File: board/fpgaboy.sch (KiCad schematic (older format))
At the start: 83 parts, among them J1 Conn_01x12, J2 Conn_01x06, J3 Micro_SD_Card_Det, J4 Conn_01x06, P1 ILI9341, P2 CONN_01X02, P3 USB_OTG, Q1 BSS816NW, SW1 SWITCH_SPST, U1 iCE40-HX8k-BG121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

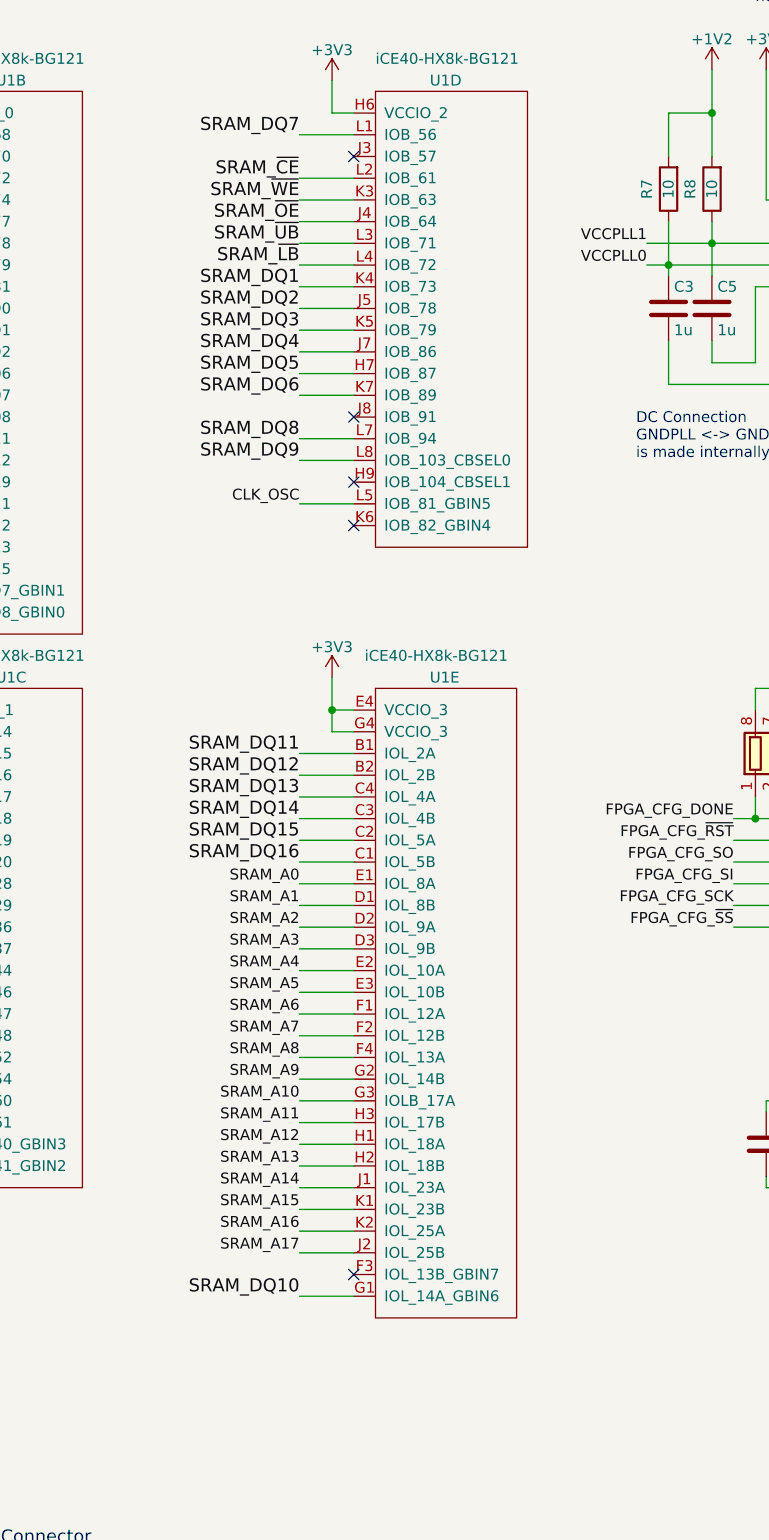
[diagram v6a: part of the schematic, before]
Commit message: Pin-swapping + routing the SRAM: 50%
Former-commit-id: 2b577cf7b52f24baabab8caba00ed91606b61012 [formerly dccfe95725d7621aa8f631ef6b86a4224c43d36a]
Former-commit-id: 66db710dd59c402621ba8271397dc92d027909e4
Former-commit-id: c62c4198c05e169013effc5fdc660d776587b68b
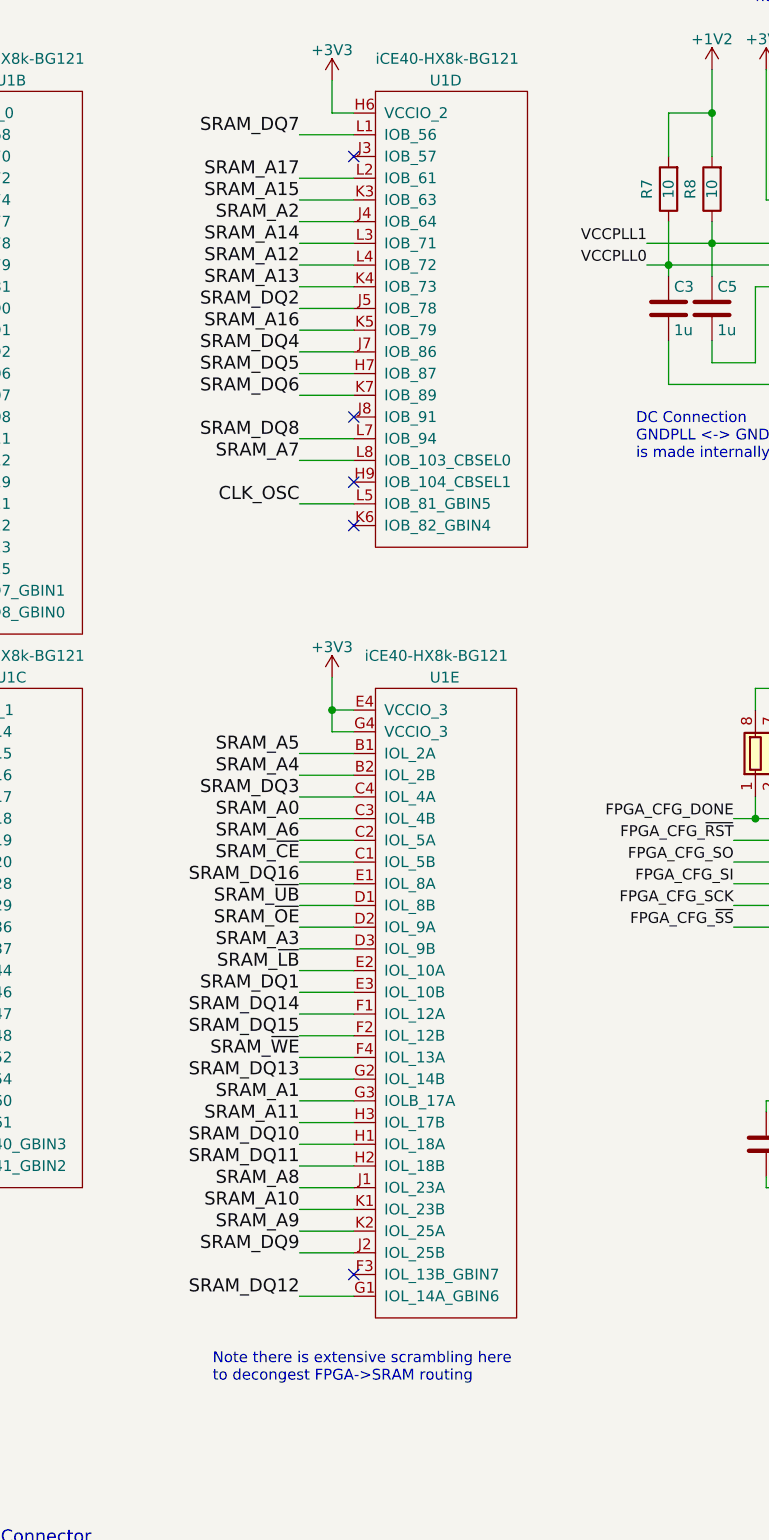
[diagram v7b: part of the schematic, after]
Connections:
- net SRAM_A0: now also U1.C3 (IOL_4B); no longer U1.E1 (IOL_8A)
- net SRAM_A1: now also U1.G3 (IOLB_17A); no longer U1.D1 (IOL_8B)
- net SRAM_A10: now also U1.K1 (IOL_23B); no longer U1.G3 (IOLB_17A)
- net SRAM_A12: now also U1.L4 (IOB_72); no longer U1.H1 (IOL_18A)
- net SRAM_A13: now also U1.K4 (IOB_73); no longer U1.H2 (IOL_18B)
- net SRAM_A14: now also U1.L3 (IOB_71); no longer U1.J1 (IOL_23A)
- net SRAM_A15: now also U1.K3 (IOB_63); no longer U1.K1 (IOL_23B)
- net SRAM_A16: now also U1.K5 (IOB_79); no longer U1.K2 (IOL_25A)
- net SRAM_A17: now also U1.L2 (IOB_61); no longer U1.J2 (IOL_25B)
- net SRAM_A2: now also U1.J4 (IOB_64); no longer U1.D2 (IOL_9A)
- net SRAM_A4: now also U1.B2 (IOL_2B); no longer U1.E2 (IOL_10A)
- net SRAM_A5: now also U1.B1 (IOL_2A); no longer U1.E3 (IOL_10B)
- net SRAM_A6: now also U1.C2 (IOL_5A); no longer U1.F1 (IOL_12A)
- net SRAM_A7: now also U1.L8 (IOB_103_CBSEL0); no longer U1.F2 (IOL_12B)
- net SRAM_A8: now also U1.J1 (IOL_23A); no longer U1.F4 (IOL_13A)
- net SRAM_A9: now also U1.K2 (IOL_25A); no longer U1.G2 (IOL_14B)
- net SRAM_DQ1: now also U1.E3 (IOL_10B); no longer U1.K4 (IOB_73)
- net SRAM_DQ10: now also U1.H1 (IOL_18A); no longer U1.G1 (IOL_14A_GBIN6)
- net SRAM_DQ11: now also U1.H2 (IOL_18B); no longer U1.B1 (IOL_2A)
- net SRAM_DQ12: now also U1.G1 (IOL_14A_GBIN6); no longer U1.B2 (IOL_2B)
- net SRAM_DQ13: now also U1.G2 (IOL_14B); no longer U1.C4 (IOL_4A)
- net SRAM_DQ14: now also U1.F1 (IOL_12A); no longer U1.C3 (IOL_4B)
- net SRAM_DQ15: now also U1.F2 (IOL_12B); no longer U1.C2 (IOL_5A)
- net SRAM_DQ16: now also U1.E1 (IOL_8A); no longer U1.C1 (IOL_5B)
- net SRAM_DQ3: now also U1.C4 (IOL_4A); no longer U1.K5 (IOB_79)
- net SRAM_DQ9: now also U1.J2 (IOL_25B); no longer U1.L8 (IOB_103_CBSEL0)
- net SRAM_~CE: now also U1.C1 (IOL_5B); no longer U1.L2 (IOB_61)
- net SRAM_~LB: now also U1.E2 (IOL_10A); no longer U1.L4 (IOB_72)
- net SRAM_~OE: now also U1.D2 (IOL_9A); no longer U1.J4 (IOB_64)
- net SRAM_~UB: now also U1.D1 (IOL_8B); no longer U1.L3 (IOB_71)
- net SRAM_~WE: now also U1.F4 (IOL_13A); no longer U1.K3 (IOB_63)
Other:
- note added: "Note there is extensive scrambling here\nto decongest FPGA->SRAM routing"
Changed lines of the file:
@@
 	1    0    0    -1
 $EndComp
-Text Label 3300 4350 2    60   ~ 0
+Text Label 3300 6250 2    60   ~ 0
 SRAM_DQ11
-Text Label 3300 4450 2    60   ~ 0
+Text Label 3300 6850 2    60   ~ 0
 SRAM_DQ12
-Text Label 3300 4550 2    60   ~ 0
+Text Label 3300 5850 2    60   ~ 0
 SRAM_DQ13
-Text Label 3300 4650 2    60   ~ 0
+Text Label 3300 5550 2    60   ~ 0
 SRAM_DQ14
-Text Label 3300 4750 2    60   ~ 0
+Text Label 3300 5650 2    60   ~ 0
 SRAM_DQ15
-Text Label 3300 4850 2    60   ~ 0
+Text Label 3300 4950 2    60   ~ 0
 SRAM_DQ16
 Wire Wire Line
@@
 	1    0    0    -1
 $EndComp
-Text Label 3300 2200 2    60   ~ 0
+Text Label 3300 5450 2    60   ~ 0
 SRAM_DQ1
 Text Label 3300 2300 2    60   ~ 0
 SRAM_DQ2
-Text Label 3300 2400 2    60   ~ 0
+Text Label 3300 4550 2    60   ~ 0
 SRAM_DQ3
 Text Label 3300 2500 2    60   ~ 0
@@
 Text Label 3300 2900 2    60   ~ 0
 SRAM_DQ8
-Text Label 3300 3000 2    60   ~ 0
+Text Label 3300 6650 2    60   ~ 0
 SRAM_DQ9
-Text Label 3300 6850 2    60   ~ 0
+Text Label 3300 6150 2    60   ~ 0
 SRAM_DQ10
 Wire Wire Line
@@
 Wire Wire Line
 	3550 6650 3300 6650
-Text Label 3300 4950 2    50   ~ 0
+Text Label 3300 4650 2    60   ~ 0
 SRAM_A0
-Text Label 3300 5050 2    50   ~ 0
+Text Label 3300 5950 2    60   ~ 0
 SRAM_A1
-Text Label 3300 5150 2    50   ~ 0
+Text Label 3300 1900 2    60   ~ 0
 SRAM_A2
-Text Label 3300 5250 2    50   ~ 0
+Text Label 3300 5250 2    60   ~ 0
 SRAM_A3
-Text Label 3300 5350 2    50   ~ 0
+Text Label 3300 4450 2    60   ~ 0
 SRAM_A4
-Text Label 3300 5450 2    50   ~ 0
+Text Label 3300 4350 2    60   ~ 0
 SRAM_A5
-Text Label 3300 5550 2    50   ~ 0
+Text Label 3300 4750 2    60   ~ 0
 SRAM_A6
-Text Label 3300 5650 2    50   ~ 0
+Text Label 3300 3000 2    60   ~ 0
 SRAM_A7
-Text Label 3300 5750 2    50   ~ 0
+Text Label 3300 6350 2    60   ~ 0
 SRAM_A8
-Text Label 3300 5850 2    50   ~ 0
+Text Label 3300 6550 2    60   ~ 0
 SRAM_A9
-Text Label 3300 5950 2    50   ~ 0
+Text Label 3300 6450 2    60   ~ 0
 SRAM_A10
-Text Label 3300 6050 2    50   ~ 0
+Text Label 3300 6050 2    60   ~ 0
 SRAM_A11
-Text Label 3300 6150 2    50   ~ 0
+Text Label 3300 2100 2    60   ~ 0
 SRAM_A12
-Text Label 3300 6250 2    50   ~ 0
+Text Label 3300 2200 2    60   ~ 0
 SRAM_A13
-Text Label 3300 6350 2    50   ~ 0
+Text Label 3300 2000 2    60   ~ 0
 SRAM_A14
-Text Label 3300 6450 2    50   ~ 0
+Text Label 3300 1800 2    60   ~ 0
 SRAM_A15
-Text Label 3300 6550 2    50   ~ 0
+Text Label 3300 2400 2    60   ~ 0
 SRAM_A16
-Text Label 3300 6650 2    50   ~ 0
+Text Label 3300 1700 2    60   ~ 0
 SRAM_A17
 Text Label 1350 4350 2    59   ~ 0
@@
 Wire Wire Line
 	3550 3200 3300 3200
-Text Label 3300 3200 2    50   ~ 0
+Text Label 3300 3200 2    60   ~ 0
 CLK_OSC
 NoConn ~ 3550 1600
@@
 Text Notes 6650 3550 0    50   ~ 0
 Separate nets from 1V2\ndue to RC filter. Must\nexplicitly mark as powered.
-Text Label 3300 1700 2    60   ~ 0
+Text Label 3300 4850 2    60   ~ 0
 SRAM_~CE
-Text Label 3300 1800 2    60   ~ 0
+Text Label 3300 5750 2    60   ~ 0
 SRAM_~WE
-Text Label 3300 1900 2    60   ~ 0
+Text Label 3300 5150 2    60   ~ 0
 SRAM_~OE
-Text Label 3300 2000 2    60   ~ 0
+Text Label 3300 5050 2    60   ~ 0
 SRAM_~UB
-Text Label 3300 2100 2    60   ~ 0
+Text Label 3300 5350 2    60   ~ 0
 SRAM_~LB
 Wire Wire Line
@@
 NoConn ~ 3550 3100
 NoConn ~ 3550 2800
+Text Notes 2900 7250 0    50   ~ 0
+Note there is extensive scrambling here\nto decongest FPGA->SRAM routing
 $EndSCHEMATC

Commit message: FPGA -> SRAM connected, still needs some tidying
Former-commit-id: 485c30751ef063f7c9d3ffd6dee203909d14fc5b [formerly 03235fb12b113a93dc78ef023ce4bd03212aa64c]
Former-commit-id: c6d7b3678d387a07fbd4eb6c1dc3e0ac1262a6cf
Former-commit-id: 99bfaaad5736dd77a389fe19bcf24d957bc4f62f
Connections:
- net SRAM_A0: now also U1.E3 (IOL_10B); no longer U1.C3 (IOL_4B)
- net SRAM_A1: now also U1.D3 (IOL_9B); no longer U1.G3 (IOLB_17A)
- net SRAM_A12: now also U1.L7 (IOB_94); no longer U1.L4 (IOB_72)
- net SRAM_A13: now also U1.K7 (IOB_89); no longer U1.K4 (IOB_73)
- net SRAM_A14: now also U1.K5 (IOB_79); no longer U1.L3 (IOB_71)
- net SRAM_A15: now also U1.L4 (IOB_72); no longer U1.K3 (IOB_63)
- net SRAM_A16: now also U1.L8 (IOB_103_CBSEL0); no longer U1.K5 (IOB_79)
- net SRAM_A17: now also U1.L1 (IOB_56); no longer U1.L2 (IOB_61)
- net SRAM_A2: now also U1.C3 (IOL_4B); no longer U1.J4 (IOB_64)
- net SRAM_A3: now also U1.C4 (IOL_4A); no longer U1.D3 (IOL_9B)
- net SRAM_A7: now also U1.C1 (IOL_5B); no longer U1.L8 (IOB_103_CBSEL0)
- net SRAM_DQ1: now also U1.G3 (IOLB_17A); no longer U1.E3 (IOL_10B)
- net SRAM_DQ2: now also U1.J4 (IOB_64); no longer U1.J5 (IOB_78)
- net SRAM_DQ3: now also U1.J5 (IOB_78); no longer U1.C4 (IOL_4A)
- net SRAM_DQ4: now also U1.H7 (IOB_87); no longer U1.J7 (IOB_86)
- net SRAM_DQ5: now also U1.J7 (IOB_86); no longer U1.H7 (IOB_87)
- net SRAM_DQ6: now also U1.L2 (IOB_61); no longer U1.K7 (IOB_89)
- net SRAM_DQ7: now also U1.K3 (IOB_63); no longer U1.L1 (IOB_56)
- net SRAM_DQ8: now also U1.L3 (IOB_71); no longer U1.L7 (IOB_94)
- net SRAM_~CE: now also U1.F4 (IOL_13A); no longer U1.C1 (IOL_5B)
- net SRAM_~WE: now also U1.K4 (IOB_73); no longer U1.F4 (IOL_13A)
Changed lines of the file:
@@
 	1    0    0    -1
 $EndComp
-Text Label 3300 5450 2    60   ~ 0
+Text Label 3300 5950 2    60   ~ 0
 SRAM_DQ1
+Text Label 3300 1900 2    60   ~ 0
+SRAM_DQ2
 Text Label 3300 2300 2    60   ~ 0
-SRAM_DQ2
-Text Label 3300 4550 2    60   ~ 0
 SRAM_DQ3
+Text Label 3300 2600 2    60   ~ 0
+SRAM_DQ4
 Text Label 3300 2500 2    60   ~ 0
-SRAM_DQ4
-Text Label 3300 2600 2    60   ~ 0
 SRAM_DQ5
-Text Label 3300 2700 2    60   ~ 0
+Text Label 3300 1700 2    60   ~ 0
 SRAM_DQ6
-Text Label 3300 1500 2    60   ~ 0
+Text Label 3300 1800 2    60   ~ 0
 SRAM_DQ7
-Text Label 3300 2900 2    60   ~ 0
+Text Label 3300 2000 2    60   ~ 0
 SRAM_DQ8
 Text Label 3300 6650 2    60   ~ 0
@@
 Wire Wire Line
 	3550 6650 3300 6650
+Text Label 3300 5450 2    60   ~ 0
+SRAM_A0
+Text Label 3300 5250 2    60   ~ 0
+SRAM_A1
 Text Label 3300 4650 2    60   ~ 0
-SRAM_A0
-Text Label 3300 5950 2    60   ~ 0
-SRAM_A1
-Text Label 3300 1900 2    60   ~ 0
 SRAM_A2
-Text Label 3300 5250 2    60   ~ 0
+Text Label 3300 4550 2    60   ~ 0
 SRAM_A3
 Text Label 3300 4450 2    60   ~ 0
@@
 Text Label 3300 4750 2    60   ~ 0
 SRAM_A6
-Text Label 3300 3000 2    60   ~ 0
+Text Label 3300 4850 2    60   ~ 0
 SRAM_A7
 Text Label 3300 6350 2    60   ~ 0
@@
 Text Label 3300 6050 2    60   ~ 0
 SRAM_A11
+Text Label 3300 2900 2    60   ~ 0
+SRAM_A12
+Text Label 3300 2700 2    60   ~ 0
+SRAM_A13
+Text Label 3300 2400 2    60   ~ 0
+SRAM_A14
 Text Label 3300 2100 2    60   ~ 0
-SRAM_A12
-Text Label 3300 2200 2    60   ~ 0
-SRAM_A13
-Text Label 3300 2000 2    60   ~ 0
-SRAM_A14
-Text Label 3300 1800 2    60   ~ 0
 SRAM_A15
-Text Label 3300 2400 2    60   ~ 0
+Text Label 3300 3000 2    60   ~ 0
 SRAM_A16
-Text Label 3300 1700 2    60   ~ 0
+Text Label 3300 1500 2    60   ~ 0
 SRAM_A17
 Text Label 1350 4350 2    59   ~ 0
@@
 Text Notes 6650 3550 0    50   ~ 0
 Separate nets from 1V2\ndue to RC filter. Must\nexplicitly mark as powered.
-Text Label 3300 4850 2    60   ~ 0
+Text Label 3300 5750 2    60   ~ 0
 SRAM_~CE
-Text Label 3300 5750 2    60   ~ 0
+Text Label 3300 2200 2    60   ~ 0
 SRAM_~WE
 Text Label 3300 5150 2    60   ~ 0
